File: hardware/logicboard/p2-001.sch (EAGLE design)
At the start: 53 parts, among them IC1 5V, IC2 4066N, IC3 LTC485N, IC4 74LS07N, J1 LEDs, J2 Display, J3 PWR, K1 G5V1, Q1 220mA/50V/3.5Ω, Q2 220mA/50V/3.5Ω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

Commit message: Silk.
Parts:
- removed RC5: 10k, resistor:R-EU_R2012
- added RZ1: Inf, resistor:R-EU_R2012
- RC3: value Inf -> 10k
- renumbered RC6 to RZ2
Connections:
- net SCL: now also RC3.1; no longer RC4.1
- net SCL3V3: now also RC4.1; no longer RC5.1
- net SDA: now also RZ1.1; no longer RC3.1
- net SDA3V3: now also RZ1.2; no longer RC3.2
- net VCC: now also RC3.2; no longer RC4.2
- net VDD: now also RC4.2; no longer RC5.2
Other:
- moved on the sheet: RC3, RC4
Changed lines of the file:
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@@
 <part name="VDD1" library="supply1" library_urn="urn:adsk.eagle:library:371" deviceset="VDD" device=""/>
 <part name="VDD2" library="supply1" library_urn="urn:adsk.eagle:library:371" deviceset="VDD" device=""/>
+<part name="RC3" library="resistor" library_urn="urn:adsk.eagle:library:348" deviceset="R-EU_" device="R2012" package3d_urn="urn:adsk.eagle:package:23543/2" value="10k"/>
 <part name="RC4" library="resistor" library_urn="urn:adsk.eagle:library:348" deviceset="R-EU_" device="R2012" package3d_urn="urn:adsk.eagle:package:23543/2" value="10k"/>
-<part name="RC5" library="resistor" library_urn="urn:adsk.eagle:library:348" deviceset="R-EU_" device="R2012" package3d_urn="urn:adsk.eagle:package:23543/2" value="10k"/>
 <part name="SUPPLY31" library="supply2" library_urn="urn:adsk.eagle:library:372" deviceset="VCC" device=""/>
 <part name="RC1" library="resistor" library_urn="urn:adsk.eagle:library:348" deviceset="R-EU_" device="R2012" package3d_urn="urn:adsk.eagle:package:23543/2" value="10k"/>
@@
 <part name="P+4" library="supply1" library_urn="urn:adsk.eagle:library:371" deviceset="+12V" device=""/>
 <part name="JV1" library="SparkFun-Connectors" library_urn="urn:adsk.eagle:library:513" deviceset="CONN_02" device="-JST-2MM-SMT" package3d_urn="urn:adsk.eagle:package:38042/1" value="DC12V"/>
-<part name="RC6" library="resistor" library_urn="urn:adsk.eagle:library:348" deviceset="R-EU_" device="R2012" package3d_urn="urn:adsk.eagle:package:23543/2" value="Inf"/>
-<part name="RC3" library="resistor" library_urn="urn:adsk.eagle:library:348" deviceset="R-EU_" device="R2012" package3d_urn="urn:adsk.eagle:package:23543/2" value="Inf"/>
+<part name="RZ2" library="resistor" library_urn="urn:adsk.eagle:library:348" deviceset="R-EU_" device="R2012" package3d_urn="urn:adsk.eagle:package:23543/2" value="Inf"/>
+<part name="RZ1" library="resistor" library_urn="urn:adsk.eagle:library:348" deviceset="R-EU_" device="R2012" package3d_urn="urn:adsk.eagle:package:23543/2" value="Inf"/>
 </parts>
 <sheets>
@@
 <attribute name="VALUE" x="182.88" y="154.94" size="1.778" layer="96" align="bottom-center"/>
 </instance>
-<instance part="RC4" gate="G$1" x="172.72" y="139.7" smashed="yes" rot="R90">
+<instance part="RC3" gate="G$1" x="172.72" y="139.7" smashed="yes" rot="R90">
 <attribute name="NAME" x="170.18" y="139.7" size="1.778" layer="95" rot="R90" align="bottom-center"/>
 <attribute name="VALUE" x="175.26" y="139.7" size="1.778" layer="96" rot="R90" align="bottom-center"/>
 </instance>
-<instance part="RC5" gate="G$1" x="187.96" y="139.7" smashed="yes" rot="R90">
+<instance part="RC4" gate="G$1" x="187.96" y="139.7" smashed="yes" rot="R90">
 <attribute name="NAME" x="185.42" y="139.7" size="1.778" layer="95" rot="R90" align="bottom-center"/>
 <attribute name="VALUE" x="190.5" y="139.7" size="1.778" layer="96" rot="R90" align="bottom-center"/>
@@
 <attribute name="NAME" x="233.68" y="30.48" size="1.778" layer="95" align="bottom-center"/>
 </instance>
-<instance part="RC6" gate="G$1" x="180.34" y="127" smashed="yes">
+<instance part="RZ2" gate="G$1" x="180.34" y="127" smashed="yes">
 <attribute name="NAME" x="180.34" y="129.54" size="1.778" layer="95" align="bottom-center"/>
 <attribute name="VALUE" x="180.34" y="124.46" size="1.778" layer="96" align="bottom-center"/>
 </instance>
-<instance part="RC3" gate="G$1" x="180.34" y="160.02" smashed="yes">
+<instance part="RZ1" gate="G$1" x="180.34" y="160.02" smashed="yes">
 <attribute name="NAME" x="180.34" y="162.56" size="1.778" layer="95" align="bottom-center"/>
 <attribute name="VALUE" x="180.34" y="157.48" size="1.778" layer="96" align="bottom-center"/>
@@
 </segment>
 <segment>
-<pinref part="RC4" gate="G$1" pin="2"/>
+<pinref part="RC3" gate="G$1" pin="2"/>
 <pinref part="SUPPLY31" gate="G$1" pin="VCC"/>
 <wire x1="172.72" y1="147.32" x2="172.72" y2="144.78" width="0.1524" layer="91"/>
@@
 <junction x="172.72" y="165.1"/>
 <label x="157.48" y="165.1" size="1.778" layer="95"/>
-<pinref part="RC3" gate="G$1" pin="1"/>
+<pinref part="RZ1" gate="G$1" pin="1"/>
 <wire x1="175.26" y1="160.02" x2="172.72" y2="160.02" width="0.1524" layer="91"/>
 <wire x1="172.72" y1="160.02" x2="172.72" y2="165.1" width="0.1524" layer="91"/>
@@
 <wire x1="157.48" y1="132.08" x2="172.72" y2="132.08" width="0.1524" layer="91"/>
 <label x="157.48" y="132.08" size="1.778" layer="95"/>
-<pinref part="RC4" gate="G$1" pin="1"/>
+<pinref part="RC3" gate="G$1" pin="1"/>
 <wire x1="172.72" y1="132.08" x2="175.26" y2="132.08" width="0.1524" layer="91"/>
 <wire x1="172.72" y1="134.62" x2="172.72" y2="132.08" width="0.1524" layer="91"/>
 <junction x="172.72" y="132.08"/>
-<pinref part="RC6" gate="G$1" pin="1"/>
+<pinref part="RZ2" gate="G$1" pin="1"/>
 <wire x1="175.26" y1="127" x2="172.72" y2="127" width="0.1524" layer="91"/>
 <wire x1="172.72" y1="127" x2="172.72" y2="132.08" width="0.1524" layer="91"/>
@@
 <pinref part="VDD2" gate="G$1" pin="VDD"/>
 <wire x1="182.88" y1="149.86" x2="182.88" y2="147.32" width="0.1524" layer="91"/>
-<pinref part="RC5" gate="G$1" pin="2"/>
+<pinref part="RC4" gate="G$1" pin="2"/>
 <wire x1="182.88" y1="147.32" x2="182.88" y2="139.7" width="0.1524" layer="91"/>
 <wire x1="187.96" y1="144.78" x2="187.96" y2="147.32" width="0.1524" layer="91"/>
@@
 <pinref part="Q2" gate="NMOS" pin="S"/>
 <wire x1="185.42" y1="132.08" x2="187.96" y2="132.08" width="0.1524" layer="91"/>
-<pinref part="RC5" gate="G$1" pin="1"/>
+<pinref part="RC4" gate="G$1" pin="1"/>
 <wire x1="187.96" y1="132.08" x2="193.04" y2="132.08" width="0.1524" layer="91"/>
 <wire x1="187.96" y1="134.62" x2="187.96" y2="132.08" width="0.1524" layer="91"/>
@@
 <wire x1="200.66" y1="162.56" x2="193.04" y2="162.56" width="0.1524" layer="91"/>
 <wire x1="193.04" y1="162.56" x2="193.04" y2="132.08" width="0.1524" layer="91"/>
-<pinref part="RC6" gate="G$1" pin="2"/>
+<pinref part="RZ2" gate="G$1" pin="2"/>
 <wire x1="185.42" y1="127" x2="187.96" y2="127" width="0.1524" layer="91"/>
 <wire x1="187.96" y1="127" x2="187.96" y2="132.08" width="0.1524" layer="91"/>
@@
 <wire x1="200.66" y1="165.1" x2="187.96" y2="165.1" width="0.1524" layer="91"/>
 <junction x="187.96" y="165.1"/>
-<pinref part="RC3" gate="G$1" pin="2"/>
+<pinref part="RZ1" gate="G$1" pin="2"/>
 <wire x1="185.42" y1="160.02" x2="187.96" y2="160.02" width="0.1524" layer="91"/>
 <wire x1="187.96" y1="160.02" x2="187.96" y2="165.1" width="0.1524" layer="91"/>

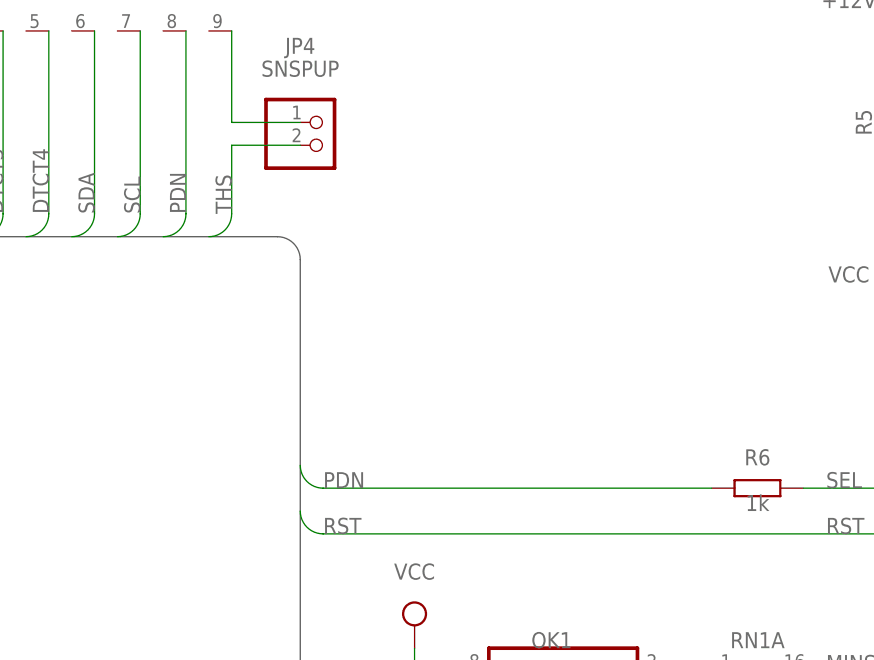
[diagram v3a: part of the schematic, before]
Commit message: Pull up of RX.
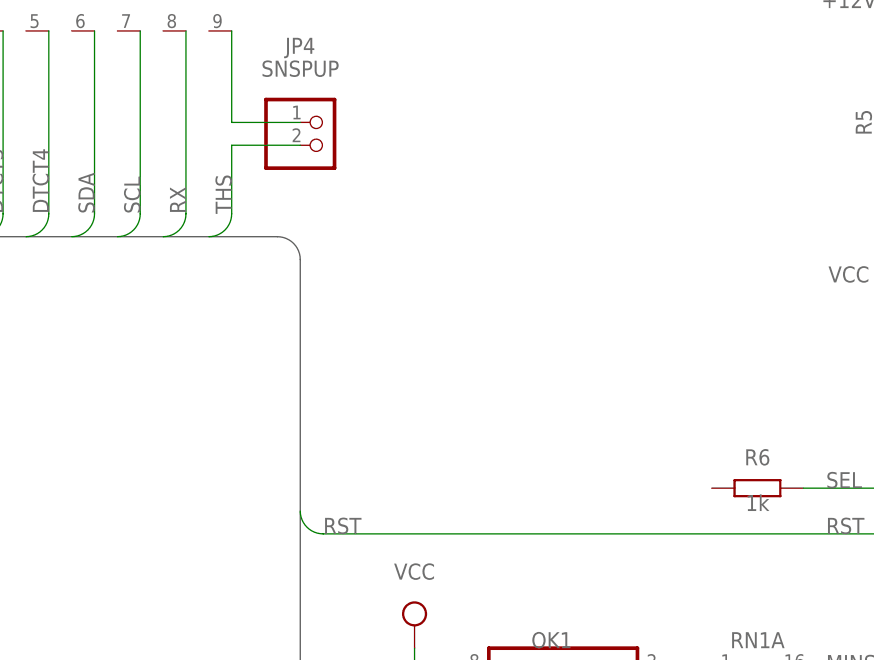
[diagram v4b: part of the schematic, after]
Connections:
- net PDN: no longer R6.1, RN2.8
- net RX: now also RN2.8
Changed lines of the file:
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@@
 <label x="274.32" y="160.02" size="1.778" layer="95"/>
+</segment>
+<segment>
+<pinref part="RN2" gate="1" pin="8"/>
+<wire x1="256.54" y1="213.36" x2="259.08" y2="215.9" width="0.1524" layer="91" curve="90"/>
+<wire x1="259.08" y1="215.9" x2="259.08" y2="236.22" width="0.1524" layer="91"/>
+<label x="259.08" y="215.9" size="1.778" layer="95" rot="R90"/>
 </segment>
 </net>
@@
 <net name="PDN" class="0">
 <segment>
-<pinref part="RN2" gate="1" pin="8"/>
-<wire x1="256.54" y1="213.36" x2="259.08" y2="215.9" width="0.1524" layer="91" curve="90"/>
-<wire x1="259.08" y1="215.9" x2="259.08" y2="236.22" width="0.1524" layer="91"/>
-<label x="259.08" y="215.9" size="1.778" layer="95" rot="R90"/>
-</segment>
-<segment>
-<pinref part="R6" gate="G$1" pin="1"/>
-<wire x1="271.78" y1="187.96" x2="274.32" y2="185.42" width="0.1524" layer="91" curve="90"/>
-<wire x1="274.32" y1="185.42" x2="317.5" y2="185.42" width="0.1524" layer="91"/>
-<label x="274.32" y="185.42" size="1.778" layer="95"/>
-</segment>
-<segment>
 <pinref part="MC1" gate="G$1" pin="A4"/>

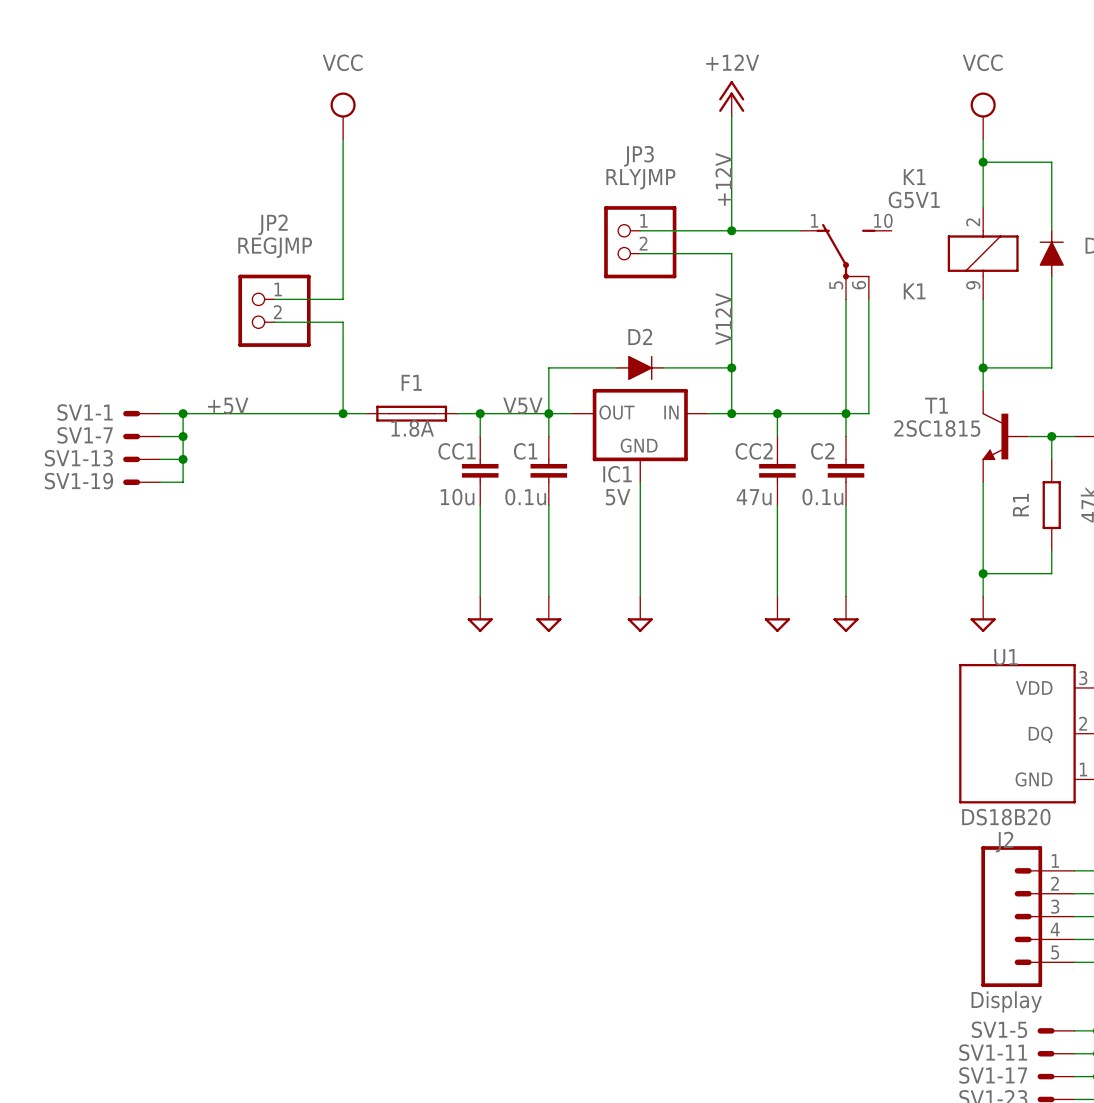
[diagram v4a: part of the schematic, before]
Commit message: Pinhead for Relay.
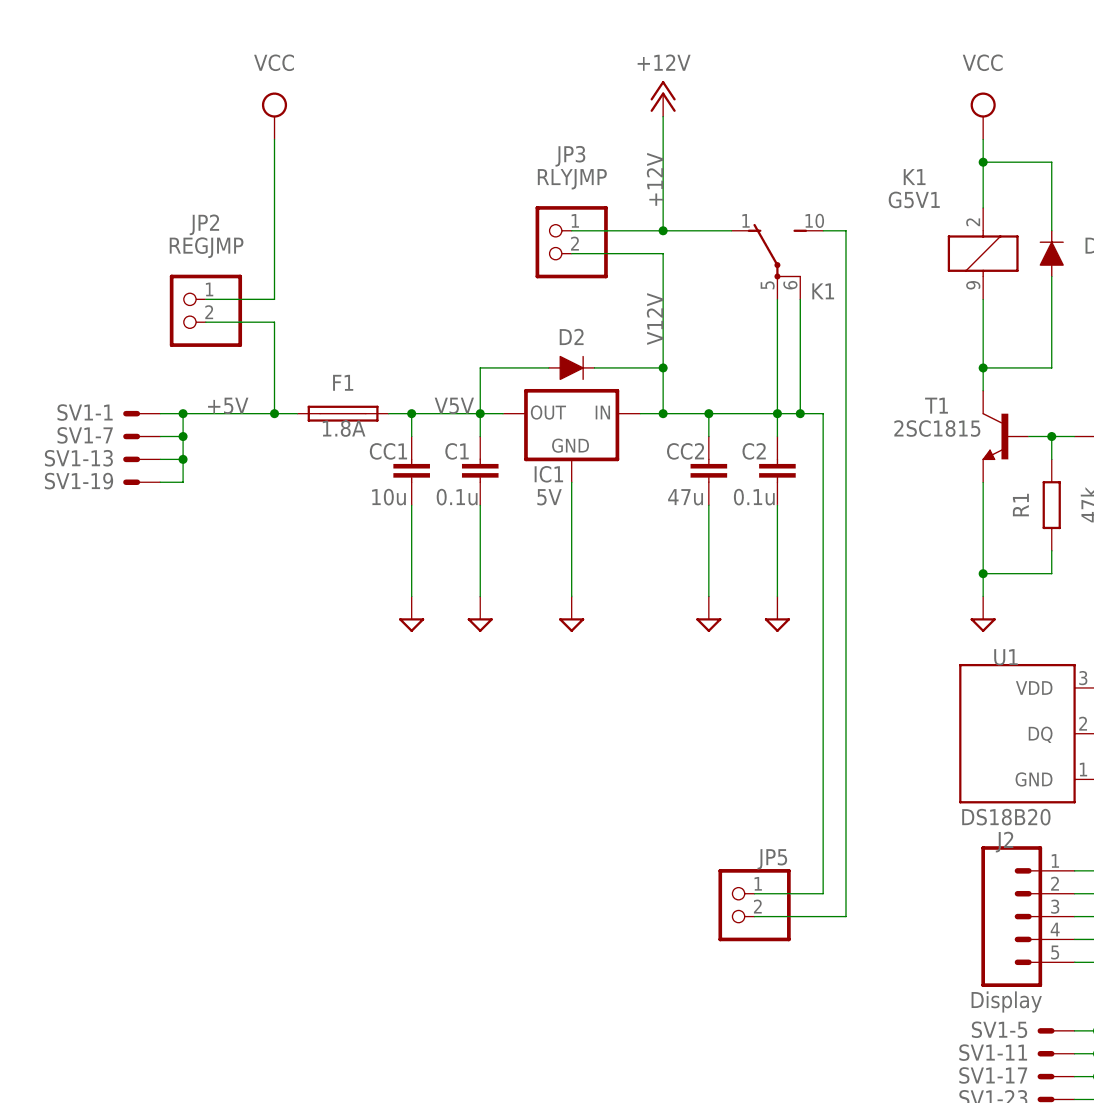
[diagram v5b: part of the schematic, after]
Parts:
- added JP5: (no value), pinhead:PINHD-1X2
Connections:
- new net N$5: JP5.2, K12.S
- net V12V: now also JP5.1
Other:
- moved on the sheet: C1, C2, CC1, CC2, D2, F1, IC1, JP2, JP3, K1

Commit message: Clean up of document, schematic, and board design.
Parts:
- JP5: value (none) -> RLY
- R6: value 1k -> 330
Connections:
- net N$1 renamed ANLG1PDN
- net N$2 renamed ANLG2PDN
- net N$3 renamed ANLG3PDN
- net N$4 renamed ANLG4PDN
- removed net SEL: R6.2, SV2-9.S
- new net N$1: R6.1, SV2-9.S
- net VCC: now also R6.2
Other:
- moved on the sheet: C2, CC2, JP5, JQ1, Q1, R6, RC1, RC2, RZ1, SV2-9

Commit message: Name of signal.
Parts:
- JP5: value RLY -> RLYOUT
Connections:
- net N$5 renamed RLYOUT
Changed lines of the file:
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@@
 <part name="RZ2" library="resistor" library_urn="urn:adsk.eagle:library:348" deviceset="R-EU_" device="R2012" package3d_urn="urn:adsk.eagle:package:23543/2" value="Inf"/>
 <part name="RZ1" library="resistor" library_urn="urn:adsk.eagle:library:348" deviceset="R-EU_" device="R2012" package3d_urn="urn:adsk.eagle:package:23543/2" value="Inf"/>
-<part name="JP5" library="pinhead" library_urn="urn:adsk.eagle:library:325" deviceset="PINHD-1X2" device="" package3d_urn="urn:adsk.eagle:package:22435/2" value="RLY"/>
+<part name="JP5" library="pinhead" library_urn="urn:adsk.eagle:library:325" deviceset="PINHD-1X2" device="" package3d_urn="urn:adsk.eagle:package:22435/2" value="RLYOUT"/>
 </parts>
 <sheets>
@@
 </segment>
 </net>
-<net name="N$5" class="0">
+<net name="RLYOUT" class="0">
 <segment>
 <pinref part="K1" gate="2" pin="S"/>
